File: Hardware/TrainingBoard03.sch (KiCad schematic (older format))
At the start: 3 parts

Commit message: made board
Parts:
- added Conn? (x2): Molex_SL_05, symbol MRDT_Connectors:Molex_SL_05
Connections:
- net labels added: +3.3V, IND_1, IND_2, IND_3, Power_Input
- wire segments 5 -> 19
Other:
- moved on the sheet: Conn?A, Conn?B, J?
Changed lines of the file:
@@
 L MRDT_Connectors:AndersonPP Conn?
 U 1 1 5F579859
-P 2900 3650
-F 0 "Conn?" H 3108 4037 60  0000 C CNN
-F 1 "AndersonPP" H 3108 3931 60  0000 C CNN
-F 2 "" H 2750 3100 60  0001 C CNN
-F 3 "" H 2750 3100 60  0001 C CNN
-	1    2900 3650
+P 3625 3825
+AR Path="/5F525D93/5F579859" Ref="Conn?"  Part="1"
+AR Path="/5F5029F1/5F579859" Ref="Conn?"  Part="1"
+F 0 "Conn?" H 3833 4212 60  0000 C CNN
+F 1 "AndersonPP" H 3833 4106 60  0000 C CNN
+F 2 "" H 3475 3275 60  0001 C CNN
+F 3 "" H 3475 3275 60  0001 C CNN
+	1    3625 3825
 	1    0    0    -1
 $EndComp
@@
 L MRDT_Connectors:AndersonPP Conn?
 U 2 1 5F57985F
-P 2900 3175
-F 0 "Conn?" H 3108 3562 60  0000 C CNN
-F 1 "AndersonPP" H 3108 3456 60  0000 C CNN
-F 2 "" H 2750 2625 60  0001 C CNN
-F 3 "" H 2750 2625 60  0001 C CNN
-	2    2900 3175
+P 3625 3350
+AR Path="/5F525D93/5F57985F" Ref="Conn?"  Part="2"
+AR Path="/5F5029F1/5F57985F" Ref="Conn?"  Part="2"
+F 0 "Conn?" H 3833 3737 60  0000 C CNN
+F 1 "AndersonPP" H 3833 3631 60  0000 C CNN
+F 2 "" H 3475 2800 60  0001 C CNN
+F 3 "" H 3475 2800 60  0001 C CNN
+	2    3625 3350
 	1    0    0    -1
 $EndComp
 Wire Wire Line
-	3300 3550 3550 3550
+	4025 3725 4275 3725
 $Comp
 L MRDT_Connectors:Test_Point J?
 U 1 1 5F579866
-P 3550 3625
-F 0 "J?" H 3600 4025 60  0000 R CNN
-F 1 "Test_Point" H 3750 3900 60  0000 R CNN
-F 2 "" H 3550 3575 60  0001 C CNN
-F 3 "" H 3550 3575 60  0001 C CNN
-	1    3550 3625
+P 4275 3800
+AR Path="/5F525D93/5F579866" Ref="J?"  Part="1"
+AR Path="/5F5029F1/5F579866" Ref="J?"  Part="1"
+F 0 "J?" H 4325 4200 60  0000 R CNN
+F 1 "Test_Point" H 4475 4075 60  0000 R CNN
+F 2 "" H 4275 3750 60  0001 C CNN
+F 3 "" H 4275 3750 60  0001 C CNN
+	1    4275 3800
 	-1   0    0    1
 $EndComp
 Wire Wire Line
-	3550 3625 3550 3550
-Connection ~ 3550 3550
+	4275 3800 4275 3725
+Connection ~ 4275 3725
 Wire Wire Line
-	3550 3550 4000 3550
+	4275 3725 4725 3725
 Wire Wire Line
-	3300 3075 4000 3075
+	4025 3250 4725 3250
 Wire Wire Line
-	4000 3550 4000 3750
+	4725 3725 4725 3925
 $Comp
 L power:GND #PWR?
 U 1 1 5F5799A6
-P 4000 3750
-F 0 "#PWR?" H 4000 3500 50  0001 C CNN
-F 1 "GND" H 4005 3577 50  0000 C CNN
-F 2 "" H 4000 3750 50  0001 C CNN
-F 3 "" H 4000 3750 50  0001 C CNN
-	1    4000 3750
+P 4725 3925
+F 0 "#PWR?" H 4725 3675 50  0001 C CNN
+F 1 "GND" H 4730 3752 50  0000 C CNN
+F 2 "" H 4725 3925 50  0001 C CNN
+F 3 "" H 4725 3925 50  0001 C CNN
+	1    4725 3925
 	1    0    0    -1
 $EndComp
+Text GLabel 4725 3250 2    50   Output ~ 0
+Power_Input
+$Comp
+L MRDT_Connectors:Molex_SL_05 Conn?
+U 1 1 5F582D81
+P 7175 4400
+F 0 "Conn?" H 7303 4708 60  0000 L CNN
+F 1 "Molex_SL_05" H 7303 4602 60  0000 L CNN
+F 2 "" H 7175 4400 60  0001 C CNN
+F 3 "" H 7175 4400 60  0001 C CNN
+	1    7175 4400
+	1    0    0    -1
+$EndComp
+Wire Wire Line
+	6975 4350 6800 4350
+Wire Wire Line
+	6800 4350 6800 4525
+$Comp
+L power:GND #PWR?
+U 1 1 5F583AFF
+P 6800 4525
+F 0 "#PWR?" H 6800 4275 50  0001 C CNN
+F 1 "GND" H 6805 4352 50  0000 C CNN
+F 2 "" H 6800 4525 50  0001 C CNN
+F 3 "" H 6800 4525 50  0001 C CNN
+	1    6800 4525
+	1    0    0    -1
+$EndComp
+Wire Wire Line
+	6425 4250 6425 4050
+$Comp
+L power:+3.3V #PWR?
+U 1 1 5F583CFB
+P 6425 4050
+F 0 "#PWR?" H 6425 3900 50  0001 C CNN
+F 1 "+3.3V" H 6440 4223 50  0000 C CNN
+F 2 "" H 6425 4050 50  0001 C CNN
+F 3 "" H 6425 4050 50  0001 C CNN
+	1    6425 4050
+	1    0    0    -1
+$EndComp
+Wire Wire Line
+	6425 4250 6975 4250
+Text GLabel 6850 4150 0    50   Input ~ 0
+IND_3
+Text GLabel 6850 4050 0    50   Input ~ 0
+IND_2
+Text GLabel 6850 3950 0    50   Input ~ 0
+IND_1
+Wire Wire Line
+	6850 3950 6975 3950
+Wire Wire Line
+	6850 4050 6975 4050
+Wire Wire Line
+	6850 4150 6975 4150
+$Comp
+L MRDT_Connectors:Molex_SL_05 Conn?
+U 1 1 5F587554
+P 7175 3225
+F 0 "Conn?" H 7303 3533 60  0000 L CNN
+F 1 "Molex_SL_05" H 7303 3427 60  0000 L CNN
+F 2 "" H 7175 3225 60  0001 C CNN
+F 3 "" H 7175 3225 60  0001 C CNN
+	1    7175 3225
+	1    0    0    -1
+$EndComp
+Wire Wire Line
+	6975 3175 6800 3175
+Wire Wire Line
+	6800 3175 6800 3350
+$Comp
+L power:GND #PWR?
+U 1 1 5F58755C
+P 6800 3350
+F 0 "#PWR?" H 6800 3100 50  0001 C CNN
+F 1 "GND" H 6805 3177 50  0000 C CNN
+F 2 "" H 6800 3350 50  0001 C CNN
+F 3 "" H 6800 3350 50  0001 C CNN
+	1    6800 3350
+	1    0    0    -1
+$EndComp
+Wire Wire Line
+	6425 3075 6425 2875
+$Comp
+L power:+3.3V #PWR?
+U 1 1 5F587563
+P 6425 2875
+F 0 "#PWR?" H 6425 2725 50  0001 C CNN
+F 1 "+3.3V" H 6440 3048 50  0000 C CNN
+F 2 "" H 6425 2875 50  0001 C CNN
+F 3 "" H 6425 2875 50  0001 C CNN
+	1    6425 2875
+	1    0    0    -1
+$EndComp
+Wire Wire Line
+	6425 3075 6975 3075
+Text GLabel 6850 2975 0    50   Input ~ 0
+IND_3
+Text GLabel 6850 2875 0    50   Input ~ 0
+IND_2
+Text GLabel 6850 2775 0    50   Input ~ 0
+IND_1
+Wire Wire Line
+	6850 2775 6975 2775
+Wire Wire Line
+	6850 2875 6975 2875
+Wire Wire Line
+	6850 2975 6975 2975
 $EndSCHEMATC

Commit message: blah blah blah
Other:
- note added: "Sheet 3: Connectors"
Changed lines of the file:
@@
 Wire Wire Line
 	6850 2975 6975 2975
+Text Notes 10200 6975 2    200  ~ 40
+Sheet 3: Connectors
 $EndSCHEMATC

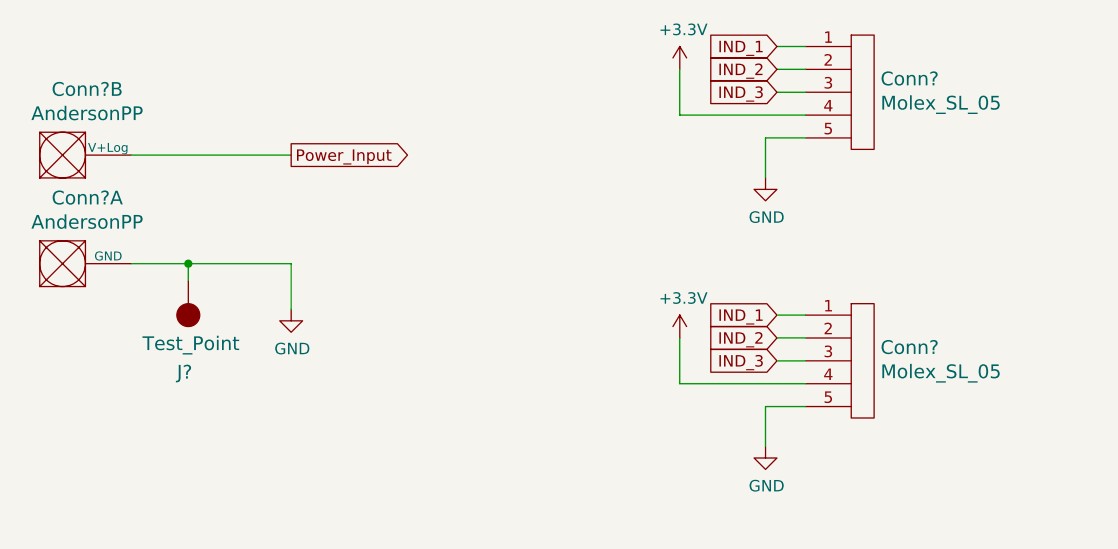
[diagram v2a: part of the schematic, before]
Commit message: Added values for buck components
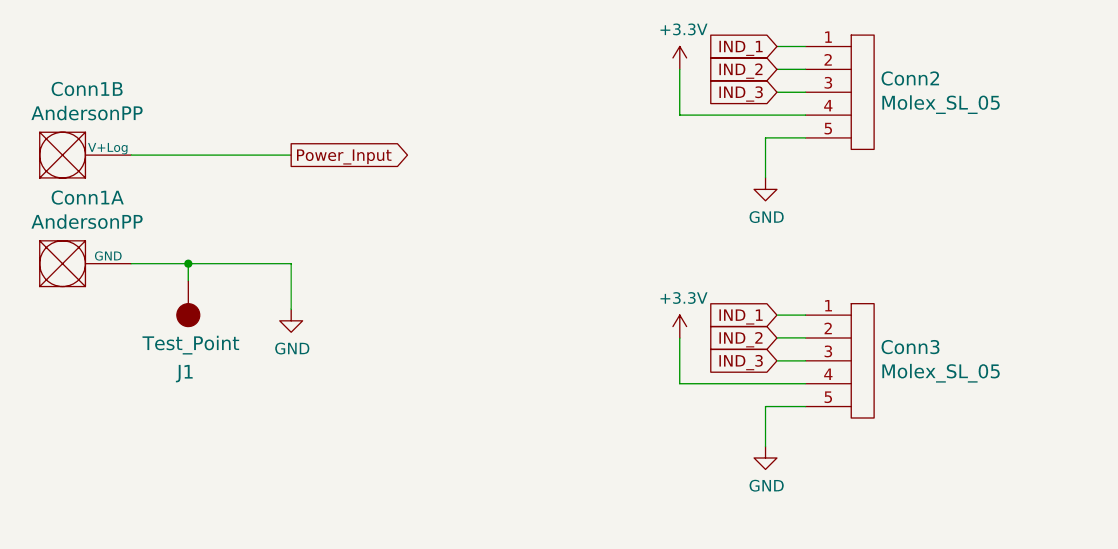
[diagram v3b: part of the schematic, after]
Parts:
- gave numbers to parts that had none: 4
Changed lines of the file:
@@
 P 3625 3825
 AR Path="/5F525D93/5F579859" Ref="Conn?"  Part="1"
-AR Path="/5F5029F1/5F579859" Ref="Conn?"  Part="1"
-F 0 "Conn?" H 3833 4212 60  0000 C CNN
+AR Path="/5F5029F1/5F579859" Ref="Conn1"  Part="1"
+F 0 "Conn1" H 3833 4212 60  0000 C CNN
 F 1 "AndersonPP" H 3833 4106 60  0000 C CNN
 F 2 "" H 3475 3275 60  0001 C CNN
@@
 P 3625 3350
 AR Path="/5F525D93/5F57985F" Ref="Conn?"  Part="2"
-AR Path="/5F5029F1/5F57985F" Ref="Conn?"  Part="2"
-F 0 "Conn?" H 3833 3737 60  0000 C CNN
+AR Path="/5F5029F1/5F57985F" Ref="Conn1"  Part="2"
+F 0 "Conn1" H 3833 3737 60  0000 C CNN
 F 1 "AndersonPP" H 3833 3631 60  0000 C CNN
 F 2 "" H 3475 2800 60  0001 C CNN
@@
 P 4275 3800
 AR Path="/5F525D93/5F579866" Ref="J?"  Part="1"
-AR Path="/5F5029F1/5F579866" Ref="J?"  Part="1"
-F 0 "J?" H 4325 4200 60  0000 R CNN
+AR Path="/5F5029F1/5F579866" Ref="J1"  Part="1"
+F 0 "J1" H 4325 4200 60  0000 R CNN
 F 1 "Test_Point" H 4475 4075 60  0000 R CNN
 F 2 "" H 4275 3750 60  0001 C CNN
@@
 	4725 3725 4725 3925
 $Comp
-L power:GND #PWR?
+L power:GND #PWR010
 U 1 1 5F5799A6
 P 4725 3925
-F 0 "#PWR?" H 4725 3675 50  0001 C CNN
+F 0 "#PWR010" H 4725 3675 50  0001 C CNN
 F 1 "GND" H 4730 3752 50  0000 C CNN
 F 2 "" H 4725 3925 50  0001 C CNN
@@
 Power_Input
 $Comp
-L MRDT_Connectors:Molex_SL_05 Conn?
+L MRDT_Connectors:Molex_SL_05 Conn3
 U 1 1 5F582D81
 P 7175 4400
-F 0 "Conn?" H 7303 4708 60  0000 L CNN
+F 0 "Conn3" H 7303 4708 60  0000 L CNN
 F 1 "Molex_SL_05" H 7303 4602 60  0000 L CNN
 F 2 "" H 7175 4400 60  0001 C CNN
@@
 	6800 4350 6800 4525
 $Comp
-L power:GND #PWR?
+L power:GND #PWR014
 U 1 1 5F583AFF
 P 6800 4525
-F 0 "#PWR?" H 6800 4275 50  0001 C CNN
+F 0 "#PWR014" H 6800 4275 50  0001 C CNN
 F 1 "GND" H 6805 4352 50  0000 C CNN
 F 2 "" H 6800 4525 50  0001 C CNN
@@
 	6425 4250 6425 4050
 $Comp
-L power:+3.3V #PWR?
+L power:+3.3V #PWR012
 U 1 1 5F583CFB
 P 6425 4050
-F 0 "#PWR?" H 6425 3900 50  0001 C CNN
+F 0 "#PWR012" H 6425 3900 50  0001 C CNN
 F 1 "+3.3V" H 6440 4223 50  0000 C CNN
 F 2 "" H 6425 4050 50  0001 C CNN
@@
 	6850 4150 6975 4150
 $Comp
-L MRDT_Connectors:Molex_SL_05 Conn?
+L MRDT_Connectors:Molex_SL_05 Conn2
 U 1 1 5F587554
 P 7175 3225
-F 0 "Conn?" H 7303 3533 60  0000 L CNN
+F 0 "Conn2" H 7303 3533 60  0000 L CNN
 F 1 "Molex_SL_05" H 7303 3427 60  0000 L CNN
 F 2 "" H 7175 3225 60  0001 C CNN
@@
 	6800 3175 6800 3350
 $Comp
-L power:GND #PWR?
+L power:GND #PWR013
 U 1 1 5F58755C
 P 6800 3350
-F 0 "#PWR?" H 6800 3100 50  0001 C CNN
+F 0 "#PWR013" H 6800 3100 50  0001 C CNN
 F 1 "GND" H 6805 3177 50  0000 C CNN
 F 2 "" H 6800 3350 50  0001 C CNN
@@
 	6425 3075 6425 2875
 $Comp
-L power:+3.3V #PWR?
+L power:+3.3V #PWR011
 U 1 1 5F587563
 P 6425 2875
-F 0 "#PWR?" H 6425 2725 50  0001 C CNN
+F 0 "#PWR011" H 6425 2725 50  0001 C CNN
 F 1 "+3.3V" H 6440 3048 50  0000 C CNN
 F 2 "" H 6425 2875 50  0001 C CNN
